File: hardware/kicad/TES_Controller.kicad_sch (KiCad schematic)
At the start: 73 parts, among them CN1 B2PS-VH, CN2 S4B-XH-A, CN3 DG381-3.5-02P-14-00A, CN5 DG381-3.5-02P-14-00A, CN6 DG381-3.5-02P-14-00A, Q1 AO3400A, Q2 AO3400A, Q3 AO3400A, Q4 AO3401A, U1 ESP32-S3-WROOM-1, U10 DG301-5.0-02P-14-00A, U12 TJA1051T_3_1J, U5 ADS1115IDGSR, U6 AMS1117-3.3, U8 LMZM23601V5SILR

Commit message: Recover the four module wire pads the extractor was silently dropping
The 120 V buck module's wires land on four pads drawn directly in copper,
not on components. PAD_NET only describes component pads, so those four
never appeared in bom.csv or netlist.txt, and I concluded from their absence
that the board had no landing point for the module's 12 V output. It has had
one all along, on every revision back to V1.

Two things that follow were wrong and are now corrected:

- The 120 V net is not a two-pad stub. It runs 63.9 mm of 1.27 mm track on
  the bottom layer from U10 across to the module's IN pad, plus 22.6 mm of
  0.25 mm feeding the divider. GND_BACK runs alongside it for 62.1 mm. That
  is a long adjacency to be holding at the current 0.152 mm clearance rule,
  and it makes the clearance fix considerably more important than "nice to
  have".
- No new terminal or solder pads need adding, and no enclosure change is
  implied.

free_pads() now emits them as W1..W4 so they are part of the netlist and DRC
can enforce a clearance class on them. They come with a symbol and a
footprint that copies V1.3's geometry exactly: 3.048 x 1.524 mm pad over a
0.914 mm hole, so the wire passes through the board rather than sitting on
a surface pad — these four wires live in a vehicle that vibrates.

Also fixed: kicad_lib.py counted easyeda2kicad's progress lines from stdout,
but the tool writes them to stderr, so a successful run reported "0 symbols"
and failed the pipeline. The library rebuild is now opt-in (--relib) since
it is committed and re-fetching 34 parts from LCSC on every run is slow and
can fail offline.

Pipeline after the change: 77 components, 222 connections, zero netlist
difference, ERC clean.

Co-Authored-By: Claude Opus 5 <noreply@anthropic.com>
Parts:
- added W1, W2, W3, W4: SOLDERPAD-1P, TES:SOLDERPAD-TH_3.0X1.5, symbol TES:SOLDERPAD-1P
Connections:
- net 120V: now also W1.1 (W)
- net 12V: now also W2.1 (W)
- net GND: now also W4.1 (W)
- net GND_BACK: now also W3.1 (W)
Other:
- note added: "模組接線"

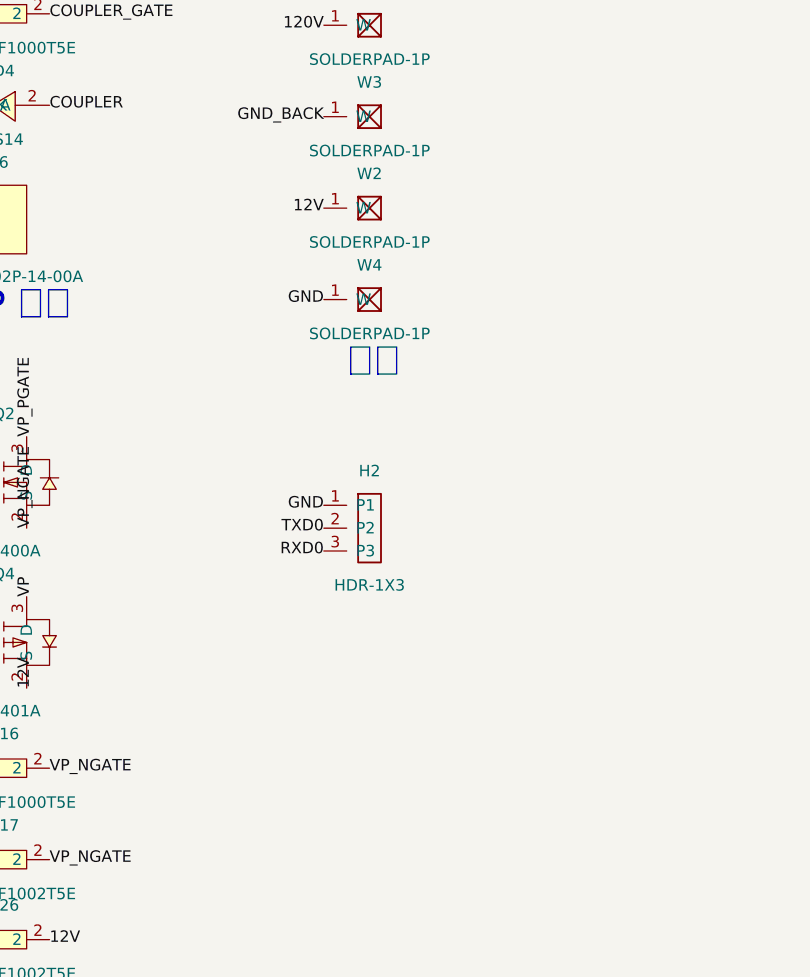
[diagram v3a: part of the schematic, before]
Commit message: Add the two TVS, and stop the copper pours from breaking connections
D9 (SMBJ130A) clamps the 120 V input, D10 (SMBJ13A) the 12 V rail. Both
reuse the SMBJ12A symbol and SMB footprint already in the library, so no new
parts were needed — only the value differs.

D9 goes at U10, the screw terminal where 120 V enters the board, not at W1
where the module's wires leave it. They are the same net, but a surge
arrives at U10 and there is 64 mm of track (~50 nH) between the two; a TVS
at W1 lets U10 rise well above the clamp, and R10 — a single 0603 rated 75 V
already sitting at 116 V — hangs off that end. It clamps to GND_BACK rather
than board ground so the surge current stays in the high-voltage loop.

13 V rather than 12 V on the rail: SMBJ12A's standoff voltage is exactly
12.0 V, so it would leak at the rail's own operating voltage once module
tolerance and ripple are included. (D3 on VP has the same issue and is worth
revisiting.)

Electrical changes are declared in tools/changes_v13.py rather than edited
in by hand, so verification survives them: the check is now "V1.3's netlist
plus the declared changes" against the board, still 226 connections and zero
difference. Each entry carries its reasoning.

The bigger find was that re-pouring kept breaking connections — a different
one or two each time. EasyEDA exports the small copper patch beside each pad
as its own zone, 233 of them at 0.01-0.05 mm2, and KiCad re-evaluates them
against its island rules on every refill. Deleting all 233 cost 3
connections to repair, which the repair pass handles. That also means every
refill the user does in the GUI would have broken something.

Three bugs in the new tooling, all found by DRC rather than by reading:
- Placement only tested courtyard overlap, so D9 landed with its 120 V pad
  0.047 mm from a 12 V track. Pad clearance is checked now, high-voltage
  rule included.
- A valid position is not a routable one: D9's first spot sat across the
  12 V trunk with no way around it. Pl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
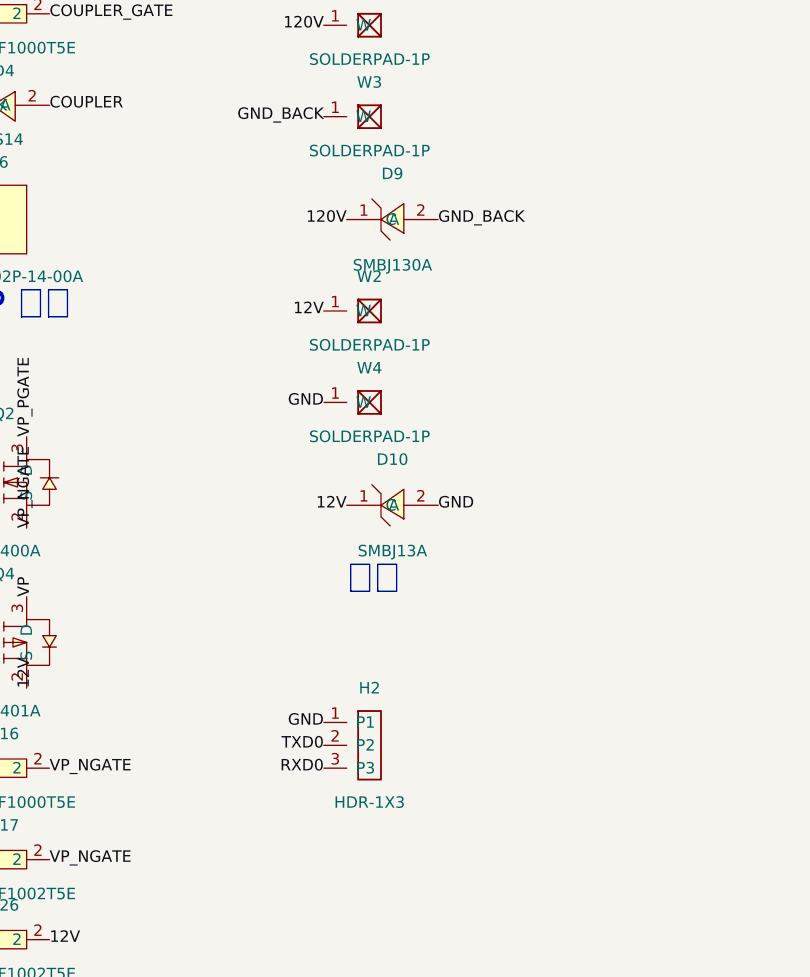
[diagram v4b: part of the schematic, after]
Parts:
- added D10: SMBJ13A, TES:SMB_L4.6-W3.6-LS5.3-RD, symbol TES:SMBJ12A_C908793
- added D9: SMBJ130A, TES:SMB_L4.6-W3.6-LS5.3-RD, symbol TES:SMBJ12A_C908793
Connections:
- net 120V: now also D9.1 (C)
- net 12V: now also D10.1 (C)
- net GND: now also D10.2 (A)
- net GND_BACK: now also D9.2 (A)

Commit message: Make the board and schematic agree on one footprint library
The board's footprints pointed at a library called TES_Contro-easyedapro
that does not exist, while the schematic assigned TES:. That is not just a
warning — the first time anyone runs "Update PCB from Schematic" in the GUI,
all 73 footprints get swapped and the routing goes with them.

Fixing it turned up something I had got wrong earlier. easyeda2kicad works
from LCSC part numbers, so it skips generic parts, and I concluded the 5 mm
LED, the 2.54 mm headers and the solder jumper had no footprints and drew
them myself. The EasyEDA Pro project zip has them all along; they came in
with the board import. The two versions differ — the LED's pin 1 is on the
opposite side and the drill is 1.00 mm rather than 0.90 — and the imported
ones are what V1.1 and V1.2 were actually built and soldered with, so those
win. tools/pcb_export_fp.py writes the board's footprints out to TES.pretty,
carrying over the 3D model references the board copies lack, and the symbols
and the footprint generator now point at them.

Dangling copper is gone too: 8 tracks, 1 via and 2 vias drilled straight
through U10's through-hole pad, the last from routing that places a via at
the start of a path when that start is already a plated hole. It took four
passes, since removing one layer of stubs exposes the next.

That clean-up also cost a connection on the first attempt. Matching the DRC
report by coordinate alone deletes every track sharing that endpoint, not
the dangling one; the report's length field distinguishes them.

The 60 remaining library mismatches are text-position differences between
rotated instances and the single canonical copy — one exported footprint
cannot match 19 differently-rotated R0603 placements. Warning only, and it
does not affect what gets fabricated.

DRC: zero errors, zero unconnected, 174 warnings. ERC clean, netlist still
226 connections with zero difference.

Co-Authored-By: Claude Opus 5 <noreply@anthropic.co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
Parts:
- D6, D7, D8: footprint TES:LED-TH_5MM -> TES:LED-TH_BD5.8-P2.54-FD
- H1: footprint TES:HDR-TH_1X4_P2.54 -> TES:HDR-TH_4P-P2.54-V-F
- H2: footprint TES:HDR-TH_1X3_P2.54 -> TES:HDR-TH_3P-P2.54-V-F

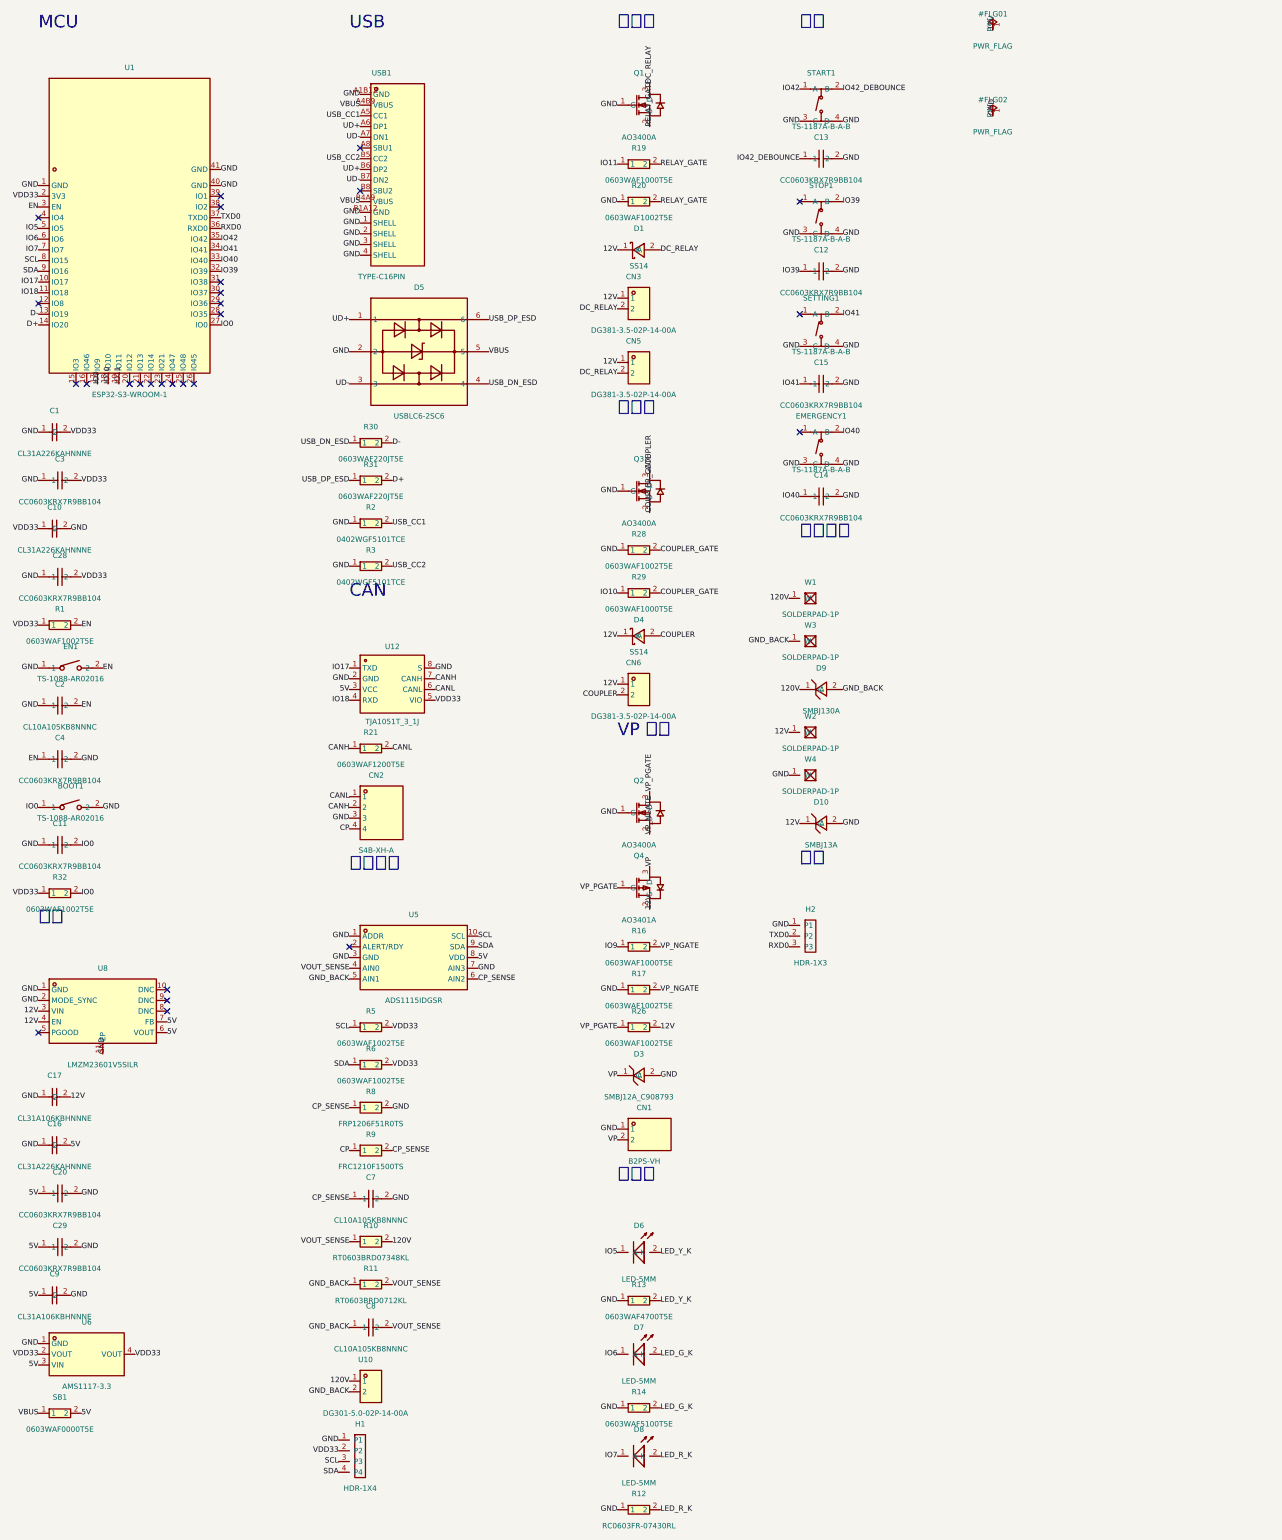
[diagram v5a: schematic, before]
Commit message: Split R10 so no resistor sits above its rated voltage
R10 is a single 0603 carrying the top half of the 120 V sense divider. A
0603's rated working voltage is 75 V; at 120 V input it sees 116 V, half
again over the limit. This is not thin margin, it is continuous operation
out of spec, and the failure mode is quiet: the resistor drifts upward,
which lowers the divided voltage, so the charger reads the pack as lower
than it is and reports that to the vehicle.

118k + 115k + 115k comes to exactly 348k, so the divider ratio is unchanged
and AIN0 still sits at 4.0000 V at 120 V input — no firmware constant moves.
All three are E96 values. Each drops 38-39 V, giving 1.9x margin on the 75 V
rating, and dissipates 13 mW against a 100 mW part.

The chain is placed as a tight vertical run up the left edge, R10 to R33 to
R34, 1.9 mm apart. Spreading series resistors out would carry 40-80 V across
the board and couple noise into the divider midpoint; the first attempt
anchored R34 to R11 and produced a 14.5 mm run, now 2.4 mm.

The two new midpoints are at 80.7 V and 42.4 V. IPC-2221B wants 0.13 mm for
those with a coating and the board default of 0.15 mm already passes, but
1.15x is not much for 80 V, so a rule holds them at 0.25 mm and the pours
back off accordingly.

Also reverted: a "fix" to the START debounce capacitor that fixed nothing.
V1.3 wires U1.35 to START1 pin 1 and C13 to pin 2, which looked inconsistent
with the other three buttons. I read that as the capacitor filtering behind
the switch's contact resistance. It is not — the TS-1187A bonds pins 1 and 2
inside the package, and 3 and 4 likewise, with the moving contact between
the two pairs. The netlist says as much: START1.3 and START1.4 both go to
GND. C13 and U1.35 are already on one solid node. Changing it only added
7.4 mm of track.

Netlist verifies at 229 connections against V1.3 plus the declared changes.
ERC and DRC both clean.

Co-Authored-By: Claude Opus 5 <noreply@anthropic.com>
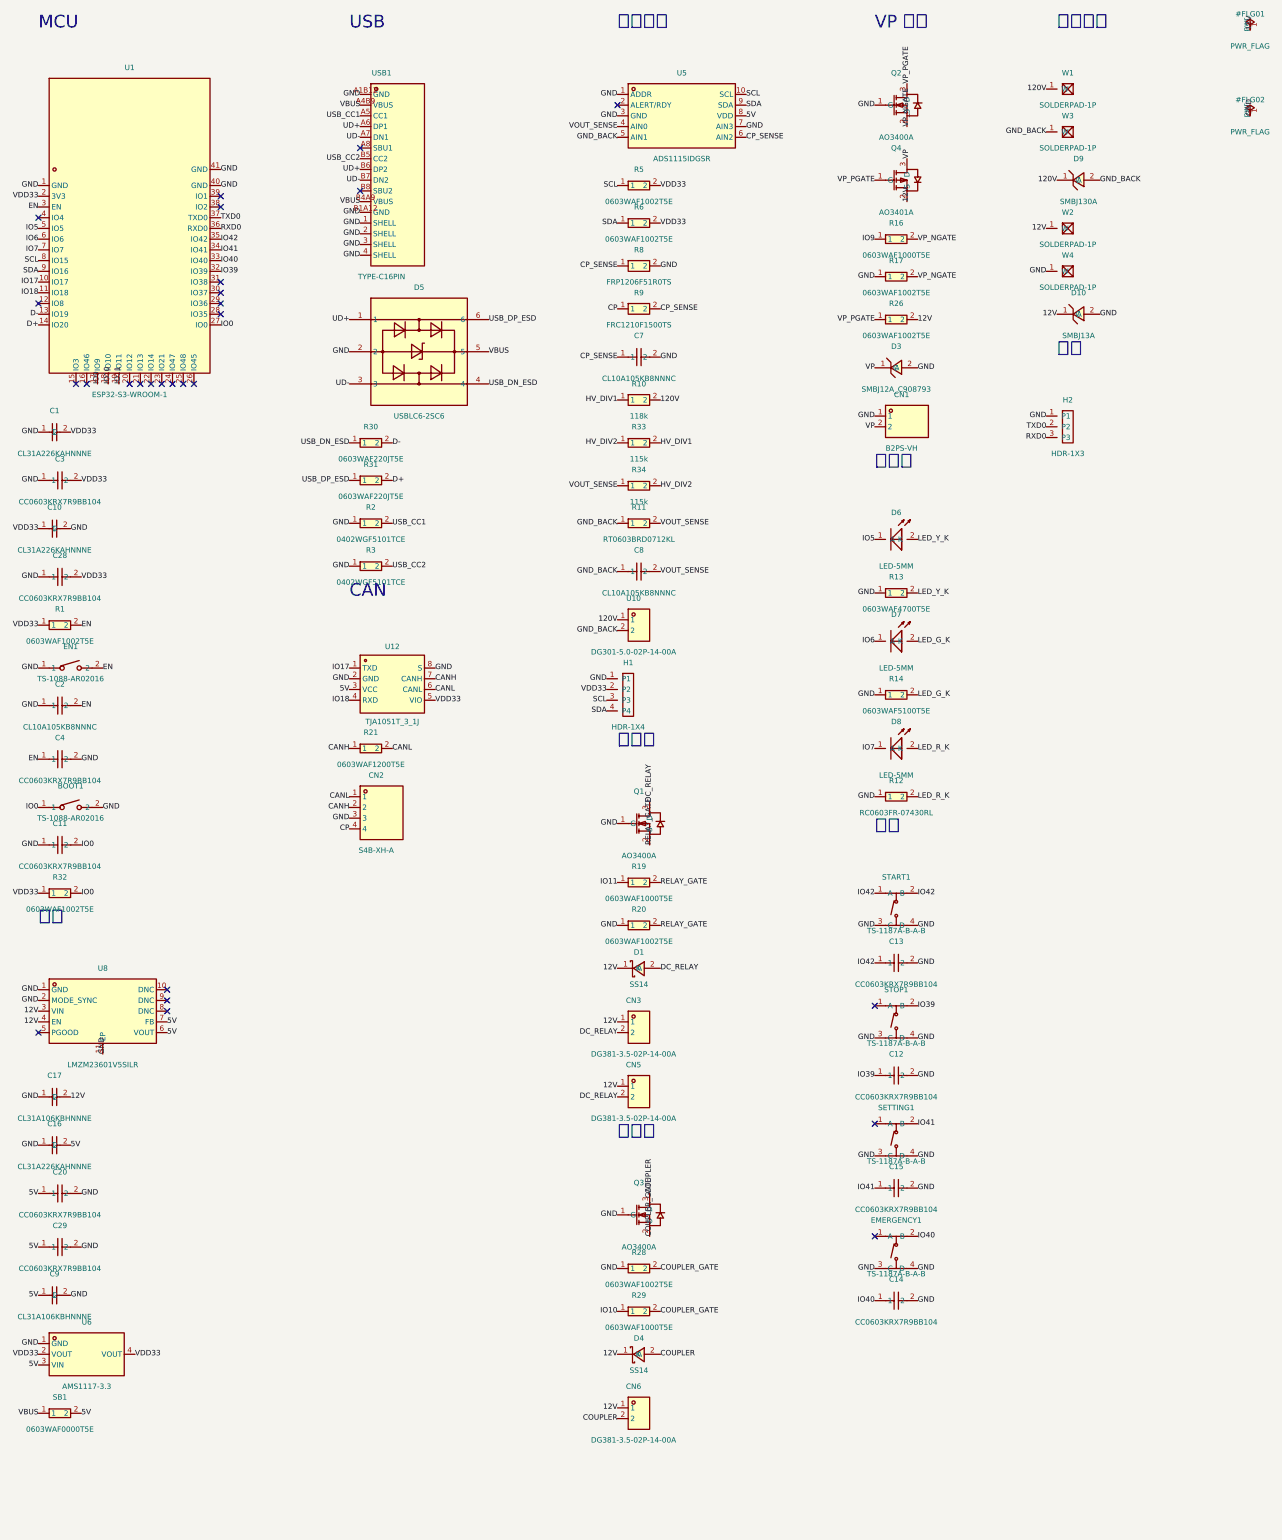
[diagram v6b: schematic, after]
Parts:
- added R33, R34: 115k, TES:R0603, symbol TES:0603WAF1002T5E
- R10: value RT0603BRD07348KL -> 118k
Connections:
- net IO42_DEBOUNCE is gone; now on net IO42: C13.1, START1.2 (B)
- net VOUT_SENSE: now also R34.1; no longer R10.1
- new net HV_DIV1: R10.1, R33.2
- new net HV_DIV2: R33.1, R34.2

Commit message: Move the ADS1115 back to 3.3 V and rescale the divider to suit
The I2C bus could not have worked reliably as drawn. The ADS1115 needs
0.7 x VDD to read a logic high — 3.50 V at a 5 V supply — while R5 and R6
pull the bus up to VDD33, so the high level is 3.3 V. Two tenths of a volt
below threshold, on a board that has not been built, so nothing has ever
exercised it. At 3.3 V the threshold drops to 2.31 V and the margin becomes
1.43x.

The reason it was at 5 V in the first place was range: V1.2 ran the part at
3.3 V and could not measure to 120 V. R11 covers that instead, 12k to
9.09k. At 120 V input AIN0 now reads 3.0547 V, inside the 3.6 V pin limit,
and the ceiling rises from 122.9 V to 141.4 V — at 5 V the PGA's 4.096 V
was the binding constraint, at 3.3 V it is the pin, and the pin is the more
generous of the two. Resolution goes from 3.750 to 4.910 mV per LSB, which
at 120 V is 0.004%.

Two consequences to carry into the firmware work:

- The divider coefficient changes from 30.000 to 39.284. This is exactly
  what the planned hw_info EEPROM is for — divider values that differ per
  hardware revision.
- CP shares this ADC through its own 150R/51R divider, so its measurement
  ceiling drops from 20.9 V to 14.2 V. Charging measured 8.99 V, leaving
  58% headroom, but if the TES spec permits 12 V that falls to 18%. Worth
  confirming against a real vehicle.

The R10 split also moves to Yageo's RT thin-film series rather than the
generic 1% parts I first used. The divider ratio *is* the voltage reading's
accuracy; three 1% resistors in the upper arm would take it from 0.1% to
about 0.58%. These part numbers follow the series' documented pattern but
need checking against LCSC stock — RT does not carry every E96 value.

Also fixed: _pcb_apply_nets ripped the tracks off any pad named in a
set_net, including ones already on the target net, which quietly
disconnected HV_DIV1 on the second run.

DRC and ERC clean, netlist 230 connections with zero difference, and all
fo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
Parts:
- R10: value 118k -> RT0603BRD07118KL
- R11: value RT0603BRD0712KL -> RT0603BRD079K09L
- R33, R34: value 115k -> RT0603BRD07115KL
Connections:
- net 5V: no longer C20.1, U5.8 (VDD)
- net IO42: no longer C13.1, START1.2 (B)
- net VDD33: now also C20.1, U5.8 (VDD)
- new net IO42_DEBOUNCE: C13.1, START1.2 (B)
